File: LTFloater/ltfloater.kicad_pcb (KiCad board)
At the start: 2 copper layers, 100.2 x 81 mm, 113 parts, among them J1 USB_C_Receptacle, J2 USB_C_Receptacle, J3 TC2030-IDC, J4 D4, J5 D5, J6 A6, J7 A7, J8 B0, K0 K00, K1 K01, K10 K10, K11 K11, K12 K12, K13 K13, K13b1 K13b, K14 K14, K2 K02, K20 K20, K21 K21, K22 K22, K23 K23, K24 K24, K3 K03, K30 K30, K31 K31, K31b1 K31, K32 K32, K33 K33, K34 K34, K34b1 K33b, K4 K04, SW1 Switch-6P-2S2T, SW2 SW_Push, U1 MCP73831, U2 MCP1700 (3.0V), U3 MCP1700 (3.3V), U4 ATXMEGA-A4U-EPAD, U5 74LVC1G34, U6 nRF24L01_module, U7 FSUSB42, U8 FSUSB42, U9 FSUSB42

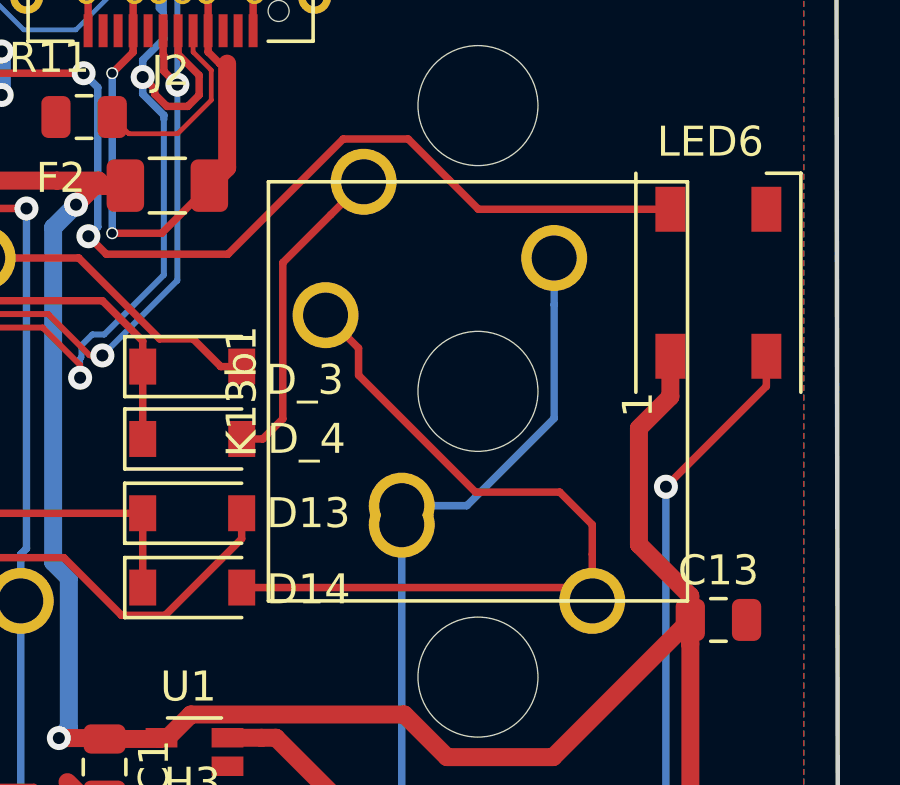
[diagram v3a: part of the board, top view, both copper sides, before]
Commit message: All switches on the one side
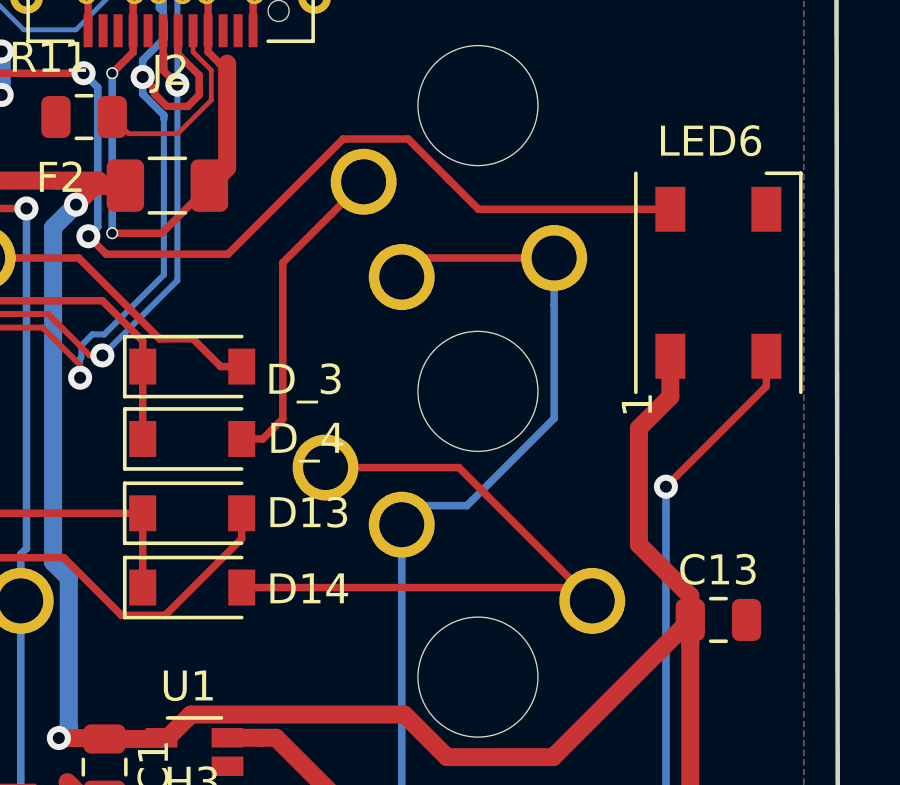
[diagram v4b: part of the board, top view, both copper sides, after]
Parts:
- K13b1: moved to B.Cu
- moved K13b1 5.08 mm to (133.8, 41.3), turned to 270 degrees
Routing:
- net /COL4: track 104.5 -> 109.8 mm
- net Net-(D14-Pad2): track 26.7 -> 22.6 mm
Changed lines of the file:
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@@
     (thickness 1.6)
     (drawings 12)
-    (tracks 1434)
+    (tracks 1431)
     (zones 0)
     (modules 113)
@@
     (uvia_drill 0.1)
   )
-  (module Button_Switch_Keyboard:SW_Cherry_MX1A_2.00u_Plate (layer F.Cu)
-    (at 133.7945 36.195 90)
+  (module Button_Switch_Keyboard:SW_Cherry_MX1A_2.00u_Plate (layer B.Cu)
+    (at 133.7945 41.275 270)
     (descr "Cherry MX keyswitch, MX1A, 2.00u, plate mount, http://cherryamericas.com/wp-content/uploads/2014/12/mx_cat.pdf")
     (tags "cherry mx keyswitch MX1A 2.00u plate")
-    (fp_text reference K13b1 (at -2.54 -2.794 90) (layer F.SilkS)
-      (effects (font (size 1 1) (thickness 0.15)))
+    (fp_text reference K13b1 (at -2.54 2.794 270) (layer B.SilkS)
+      (effects (font (size 1 1) (thickness 0.15)) (justify mirror))
     )
-    (fp_text value K13b (at -2.54 12.954 90) (layer F.Fab)
-      (effects (font (size 1 1) (thickness 0.15)))
+    (fp_text value K13b (at -2.54 -12.954 270) (layer B.Fab)
+      (effects (font (size 1 1) (thickness 0.15)) (justify mirror))
     )
-    (fp_text user %R (at -2.54 -2.794 90) (layer F.Fab)
-      (effects (font (size 1 1) (thickness 0.15)))
+    (fp_text user %R (at -2.54 2.794 270) (layer B.Fab)
+      (effects (font (size 1 1) (thickness 0.15)) (justify mirror))
     )
-    (fp_line (start -8.89 -1.27) (end 3.81 -1.27) (layer F.Fab) (width 0.15))
-    (fp_line (start 3.81 -1.27) (end 3.81 11.43) (layer F.Fab) (width 0.15))
-    (fp_line (start 3.81 11.43) (end -8.89 11.43) (layer F.Fab) (width 0.15))
-    (fp_line (start -8.89 11.43) (end -8.89 -1.27) (layer F.Fab) (width 0.15))
-    (fp_line (start -9.14 11.68) (end -9.14 -1.52) (layer F.CrtYd) (width 0.05))
-    (fp_line (start 4.06 11.68) (end -9.14 11.68) (layer F.CrtYd) (width 0.05))
-    (fp_line (start 4.06 -1.52) (end 4.06 11.68) (layer F.CrtYd) (width 0.05))
-    (fp_line (start -9.14 -1.52) (end 4.06 -1.52) (layer F.CrtYd) (width 0.05))
-    (fp_line (start -21.59 -4.445) (end 16.51 -4.445) (layer Dwgs.User) (width 0.15))
-    (fp_line (start 16.51 -4.445) (end 16.51 14.605) (layer Dwgs.User) (width 0.15))
-    (fp_line (start 16.51 14.605) (end -21.59 14.605) (layer Dwgs.User) (width 0.15))
-    (fp_line (start -21.59 14.605) (end -21.59 -4.445) (layer Dwgs.User) (width 0.15))
-    (fp_line (start -9.525 -1.905) (end 4.445 -1.905) (layer F.SilkS) (width 0.12))
-    (fp_line (start 4.445 -1.905) (end 4.445 12.065) (layer F.SilkS) (width 0.12))
-    (fp_line (start 4.445 12.065) (end -9.525 12.065) (layer F.SilkS) (width 0.12))
-    (fp_line (start -9.525 12.065) (end -9.525 -1.905) (layer F.SilkS) (width 0.12))
-    (pad 1 thru_hole circle (at 0 0 90) (size 2.2 2.2) (drill 1.5) (layers *.Cu *.Mask)
+    (fp_line (start -8.89 1.27) (end 3.81 1.27) (layer B.Fab) (width 0.15))
+    (fp_line (start 3.81 1.27) (end 3.81 -11.43) (layer B.Fab) (width 0.15))
+    (fp_line (start 3.81 -11.43) (end -8.89 -11.43) (layer B.Fab) (width 0.15))
+    (fp_line (start -8.89 -11.43) (end -8.89 1.27) (layer B.Fab) (width 0.15))
+    (fp_line (start -9.14 -11.68) (end -9.14 1.52) (layer B.CrtYd) (width 0.05))
+    (fp_line (start 4.06 -11.68) (end -9.14 -11.68) (layer B.CrtYd) (width 0.05))
+    (fp_line (start 4.06 1.52) (end 4.06 -11.68) (layer B.CrtYd) (width 0.05))
+    (fp_line (start -9.14 1.52) (end 4.06 1.52) (layer B.CrtYd) (width 0.05))
+    (fp_line (start -21.59 4.445) (end 16.51 4.445) (layer Dwgs.User) (width 0.15))
+    (fp_line (start 16.51 4.445) (end 16.51 -14.605) (layer Dwgs.User) (width 0.15))
+    (fp_line (start 16.51 -14.605) (end -21.59 -14.605) (layer Dwgs.User) (width 0.15))
+    (fp_line (start -21.59 -14.605) (end -21.59 4.445) (layer Dwgs.User) (width 0.15))
+    (fp_line (start -9.525 1.905) (end 4.445 1.905) (layer B.SilkS) (width 0.12))
+    (fp_line (start 4.445 1.905) (end 4.445 -12.065) (layer B.SilkS) (width 0.12))
+    (fp_line (start 4.445 -12.065) (end -9.525 -12.065) (layer B.SilkS) (width 0.12))
+    (fp_line (start -9.525 -12.065) (end -9.525 1.905) (layer B.SilkS) (width 0.12))
+    (pad 1 thru_hole circle (at 0 0 270) (size 2.2 2.2) (drill 1.5) (layers *.Cu *.Mask)
       (net 11 "Net-(D14-Pad2)"))
-    (pad 2 thru_hole circle (at -6.35 2.54 90) (size 2.2 2.2) (drill 1.5) (layers *.Cu *.Mask)
+    (pad 2 thru_hole circle (at -6.35 -2.54 270) (size 2.2 2.2) (drill 1.5) (layers *.Cu *.Mask)
       (net 92 /COL4))
-    (pad "" np_thru_hole circle (at -2.54 5.08 90) (size 4 4) (drill 4) (layers *.Cu *.Mask))
+    (pad "" np_thru_hole circle (at -2.54 -5.08 270) (size 4 4) (drill 4) (layers *.Cu *.Mask))
     (model ${KISYS3DMOD}/Button_Switch_Keyboard.3dshapes/SW_Cherry_MX1A_2.00u_Plate.wrl
       (at (xyz 0 0 0))
@@
   (segment (start 142.24 45.2755) (end 142.6845 45.72) (width 0.25) (layer F.Cu) (net 11))
   (segment (start 131.0005 45.2755) (end 142.24 45.2755) (width 0.25) (layer F.Cu) (net 11))
-  (segment (start 142.6845 44.164366) (end 142.6845 45.72) (width 0.25) (layer F.Cu) (net 11))
-  (segment (start 142.6845 43.17859) (end 142.6845 44.164366) (width 0.25) (layer F.Cu) (net 11))
-  (segment (start 141.600901 42.094991) (end 142.6845 43.17859) (width 0.25) (layer F.Cu) (net 11))
-  (segment (start 138.793489 42.094991) (end 141.600901 42.094991) (width 0.25) (layer F.Cu) (net 11))
-  (segment (start 134.894499 38.196001) (end 138.793489 42.094991) (width 0.25) (layer F.Cu) (net 11))
-  (segment (start 134.894499 37.294999) (end 134.894499 38.196001) (width 0.25) (layer F.Cu) (net 11))
-  (segment (start 133.7945 36.195) (end 134.894499 37.294999) (width 0.25) (layer F.Cu) (net 11))
+  (segment (start 138.2395 41.275) (end 142.6845 45.72) (width 0.25) (layer F.Cu) (net 11))
+  (segment (start 133.7945 41.275) (end 138.2395 41.275) (width 0.25) (layer F.Cu) (net 11))
   (segment (start 62.4205 75.184) (end 65.2145 72.39) (width 0.25) (layer F.Cu) (net 12))
   (segment (start 60.071 75.184) (end 62.4205 75.184) (width 0.25) (layer F.Cu) (net 12))
@@
   (segment (start 138.505502 42.545) (end 141.4145 39.636002) (width 0.25) (layer B.Cu) (net 92))
   (segment (start 136.3345 42.545) (end 138.505502 42.545) (width 0.25) (layer B.Cu) (net 92))
+  (segment (start 136.9695 34.29) (end 136.3345 34.925) (width 0.25) (layer F.Cu) (net 92))
+  (segment (start 141.4145 34.29) (end 136.9695 34.29) (width 0.25) (layer F.Cu) (net 92))
   (segment (start 80.04 93.7915) (end 80.04 93.9165) (width 0.25) (layer F.Cu) (net 93))
   (segment (start 79.4665 93.218) (end 80.04 93.7915) (width 0.25) (layer F.Cu) (net 93))

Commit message: Before adding rotary encoders
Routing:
- net +5V: track 341.9 -> 335.3 mm, vias 8 -> 4
- net Net-(LED3-Pad2): track 52.4 -> 46.5 mm, vias 2 -> 0
